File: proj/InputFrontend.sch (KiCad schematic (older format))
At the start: 22 parts

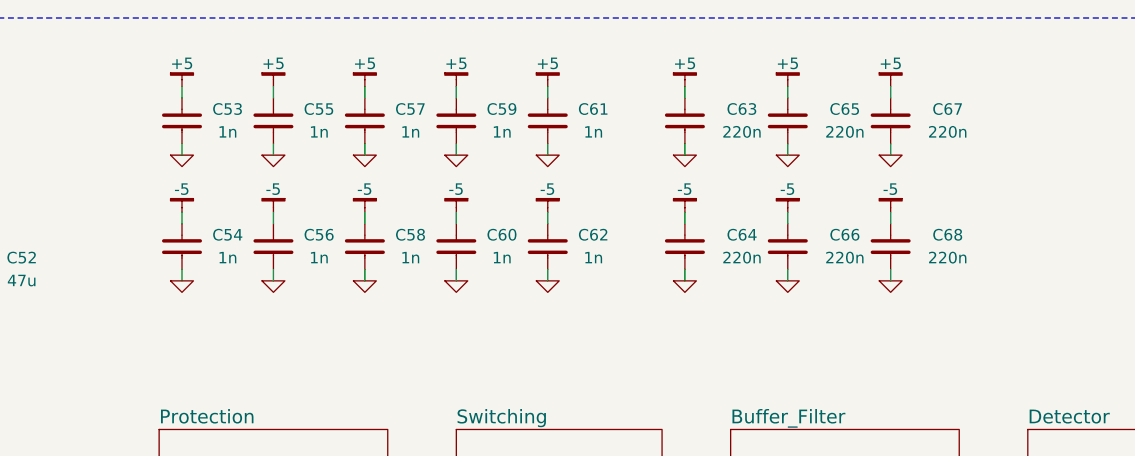
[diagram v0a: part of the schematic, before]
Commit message: All parts placed
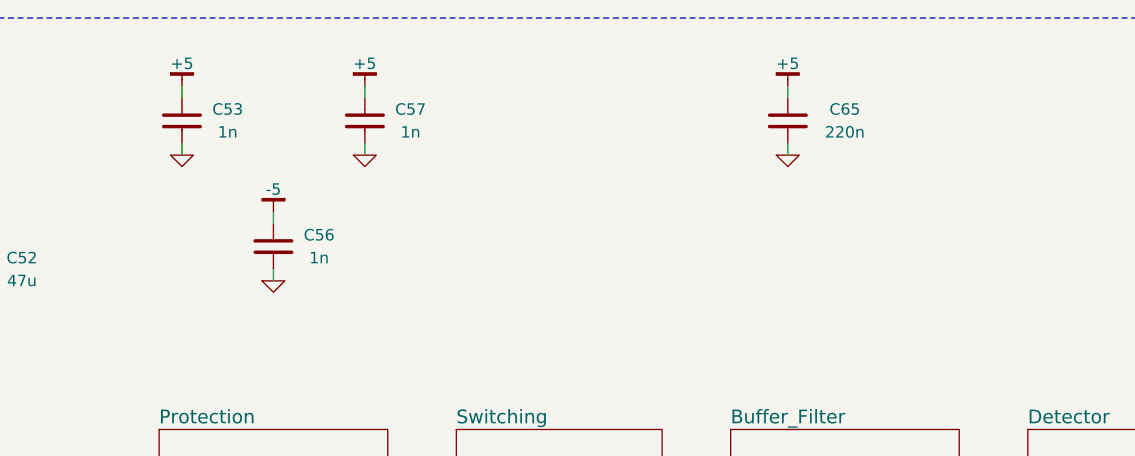
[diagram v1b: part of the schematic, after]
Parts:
- removed C54, C55, C58, C59, C60, C61, C62: 1n, IPC7351-Nominal:CAPC1005X55, symbol C-0402
- removed C63, C64, C66, C67, C68: 220n, IPC7351-Nominal:CAPC2012X70, symbol C-0805

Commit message: Major layout work - almost done
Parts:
- removed C56, C57: 1n, IPC7351-Nominal:CAPC1005X55, symbol C-0402
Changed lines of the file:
@@
 	3500 2450 3500 2400
-$Comp
-L C-0402 C56
-U 1 1 54F286AA
-P 4800 2200
-F 0 "C56" H 5000 2250 50  0000 C CNN
-F 1 "1n" H 5000 2150 50  0000 C CNN
-F 2 "IPC7351-Nominal:CAPC1005X55" H 4800 2200 50  0001 C CNN
-F 3 "" H 4790 2175 60  0000 C CNN
-F 4 "Value" H 4800 2200 60  0001 C CNN "Manuf"
-F 5 "CAP MLCC 1nF C0G 10V 5% [0402]" H 5600 2750 60  0001 C CNN "BOM"
-	1    4800 2200
-	1    0    0    -1
-$EndComp
-$Comp
-L -5 #PWR0183
-U 1 1 54F286B0
-P 4800 2050
-F 0 "#PWR0183" H 4800 2000 30  0001 C CNN
-F 1 "-5" H 4800 1950 50  0000 C CNN
-F 2 "" H 4800 2050 60  0000 C CNN
-F 3 "" H 4800 2050 60  0000 C CNN
-	1    4800 2050
-	-1   0    0    1
-$EndComp
-Wire Wire Line
-	4800 2050 4800 2100
-$Comp
-L GND #PWR0184
-U 1 1 54F286B7
-P 4800 2350
-F 0 "#PWR0184" H 4800 2350 30  0001 C CNN
-F 1 "GND" H 4800 2280 30  0001 C CNN
-F 2 "" H 4800 2350 60  0000 C CNN
-F 3 "" H 4800 2350 60  0000 C CNN
-	1    4800 2350
-	1    0    0    -1
-$EndComp
-Wire Wire Line
-	4800 2350 4800 2300
 $Comp
 L C-0402 C53
@@
 	4400 1500 4400 1550
 $Comp
-L GND #PWR0191
+L GND #PWR0181
 U 1 1 54F288BE
 P 4400 1800
-F 0 "#PWR0191" H 4400 1800 30  0001 C CNN
+F 0 "#PWR0181" H 4400 1800 30  0001 C CNN
 F 1 "GND" H 4400 1730 30  0001 C CNN
 F 2 "" H 4400 1800 60  0000 C CNN
@@
 	4400 1800 4400 1750
 $Comp
-L +5 #PWR0192
+L +5 #PWR0182
 U 1 1 54F2892E
 P 4400 1500
-F 0 "#PWR0192" H 4400 1550 30  0001 C CNN
+F 0 "#PWR0182" H 4400 1550 30  0001 C CNN
 F 1 "+5" H 4400 1600 50  0000 C CNN
 F 2 "" H 4400 1500 60  0000 C CNN
 F 3 "" H 4400 1500 60  0000 C CNN
 	1    4400 1500
-	1    0    0    -1
-$EndComp
-$Comp
-L C-0402 C57
-U 1 1 54F28B5B
-P 5200 1650
-F 0 "C57" H 5400 1700 50  0000 C CNN
-F 1 "1n" H 5400 1600 50  0000 C CNN
-F 2 "IPC7351-Nominal:CAPC1005X55" H 5200 1650 50  0001 C CNN
-F 3 "" H 5190 1625 60  0000 C CNN
-F 4 "Value" H 5200 1650 60  0001 C CNN "Manuf"
-F 5 "CAP MLCC 1nF C0G 10V 5% [0402]" H 6000 2200 60  0001 C CNN "BOM"
-	1    5200 1650
-	1    0    0    -1
-$EndComp
-Wire Wire Line
-	5200 1500 5200 1550
-$Comp
-L GND #PWR0195
-U 1 1 54F28B62
-P 5200 1800
-F 0 "#PWR0195" H 5200 1800 30  0001 C CNN
-F 1 "GND" H 5200 1730 30  0001 C CNN
-F 2 "" H 5200 1800 60  0000 C CNN
-F 3 "" H 5200 1800 60  0000 C CNN
-	1    5200 1800
-	1    0    0    -1
-$EndComp
-Wire Wire Line
-	5200 1800 5200 1750
-$Comp
-L +5 #PWR0196
-U 1 1 54F28B69
-P 5200 1500
-F 0 "#PWR0196" H 5200 1550 30  0001 C CNN
-F 1 "+5" H 5200 1600 50  0000 C CNN
-F 2 "" H 5200 1500 60  0000 C CNN
-F 3 "" H 5200 1500 60  0000 C CNN
-	1    5200 1500
 	1    0    0    -1
 $EndComp
@@
 	7050 1500 7050 1550
 $Comp
-L GND #PWR0209
+L GND #PWR0183
 U 1 1 54F29C50
 P 7050 1800
-F 0 "#PWR0209" H 7050 1800 30  0001 C CNN
+F 0 "#PWR0183" H 7050 1800 30  0001 C CNN
 F 1 "GND" H 7050 1730 30  0001 C CNN
 F 2 "" H 7050 1800 60  0000 C CNN
@@
 	7050 1800 7050 1750
 $Comp
-L +5 #PWR0210
+L +5 #PWR0184
 U 1 1 54F29C57
 P 7050 1500
-F 0 "#PWR0210" H 7050 1550 30  0001 C CNN
+F 0 "#PWR0184" H 7050 1550 30  0001 C CNN
 F 1 "+5" H 7050 1600 50  0000 C CNN
 F 2 "" H 7050 1500 60  0000 C CNN

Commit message: Swap 0402 to 0603, add USB inrush protection
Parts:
- removed C53, C69, C70: 1n, IPC7351-Nominal:CAPC1005X55, symbol C-0402
- removed R52, R53: 49R9, IPC7351-Nominal:RESC1005X40, symbol R-0402
- added C53: 1n, IPC7351-Nominal:CAPC1608X55, symbol C-0603
- added C69, C70: 10n, IPC7351-Nominal:CAPC1608X55, symbol C-0603
- added R52, R53: 49R9, IPC7351-Nominal:RESC1608X50, symbol R-0603
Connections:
- net +5: now also C53.1
- net Detector/OUT: now also R52.2
- net GND: now also C53.2, C69.2, C70.2
- net OUT: now also R53.1
- new net: C69.1, C70.1, R52.1, R53.2
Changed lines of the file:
@@
 $EndComp
 $Comp
-L GND #PWR0154
+L GND #PWR0147
 U 1 1 54F2F4A0
 P 3500 4300
-F 0 "#PWR0154" H 3500 4300 30  0001 C CNN
+F 0 "#PWR0147" H 3500 4300 30  0001 C CNN
 F 1 "GND" H 3500 4230 30  0001 C CNN
 F 2 "" H 3500 4300 60  0000 C CNN
@@
 Wire Notes Line
 	10300 1200 3200 1200
-$Comp
-L R-0402 R52
-U 1 1 54F300EB
-P 9600 3400
-F 0 "R52" V 9400 3400 50  0000 C CNN
-F 1 "49R9" V 9500 3400 50  0000 C CNN
-F 2 "IPC7351-Nominal:RESC1005X40" H 9600 3400 50  0001 C CNN
-F 3 "" H 9600 3450 60  0000 C CNN
-F 4 "Value" H 9600 3400 60  0001 C CNN "Manuf"
-F 5 "RES SMD 49R9 1% [0402]" H 10350 3950 60  0001 C CNN "BOM"
-	1    9600 3400
-	0    1    1    0
-$EndComp
-$Comp
-L C-0402 C69
-U 1 1 54F3060B
-P 9800 3600
-F 0 "C69" H 10000 3650 50  0000 C CNN
-F 1 "1n" H 10000 3550 50  0000 C CNN
-F 2 "IPC7351-Nominal:CAPC1005X55" H 9800 3600 50  0001 C CNN
-F 3 "" H 9790 3575 60  0000 C CNN
-F 4 "Value" H 9800 3600 60  0001 C CNN "Manuf"
-F 5 "CAP MLCC 1nF C0G 10V 5% [0402]" H 10600 4150 60  0001 C CNN "BOM"
-	1    9800 3600
-	1    0    0    -1
-$EndComp
 Wire Wire Line
 	9700 3400 10800 3400
@@
 	9800 3400 9800 3500
 Connection ~ 9800 3400
-$Comp
-L C-0402 C70
-U 1 1 54F3063B
-P 10700 3600
-F 0 "C70" H 10900 3650 50  0000 C CNN
-F 1 "1n" H 10900 3550 50  0000 C CNN
-F 2 "IPC7351-Nominal:CAPC1005X55" H 10700 3600 50  0001 C CNN
-F 3 "" H 10690 3575 60  0000 C CNN
-F 4 "Value" H 10700 3600 60  0001 C CNN "Manuf"
-F 5 "CAP MLCC 1nF C0G 10V 5% [0402]" H 11500 4150 60  0001 C CNN "BOM"
-	1    10700 3600
-	1    0    0    -1
-$EndComp
 Wire Wire Line
 	10700 3400 10700 3500
-$Comp
-L R-0402 R53
-U 1 1 54F30671
-P 10900 3400
-F 0 "R53" V 10700 3400 50  0000 C CNN
-F 1 "49R9" V 10800 3400 50  0000 C CNN
-F 2 "IPC7351-Nominal:RESC1005X40" H 10900 3400 50  0001 C CNN
-F 3 "" H 10900 3450 60  0000 C CNN
-F 4 "Value" H 10900 3400 60  0001 C CNN "Manuf"
-F 5 "RES SMD 49R9 1% [0402]" H 11650 3950 60  0001 C CNN "BOM"
-	1    10900 3400
-	0    1    1    0
-$EndComp
 Connection ~ 10700 3400
 Text HLabel 11600 3400 2    60   Output ~ 0
@@
 	11600 3400 11000 3400
 $Comp
-L GND #PWR0155
+L GND #PWR0148
 U 1 1 54F3075A
 P 9800 3800
-F 0 "#PWR0155" H 9800 3800 30  0001 C CNN
+F 0 "#PWR0148" H 9800 3800 30  0001 C CNN
 F 1 "GND" H 9800 3730 30  0001 C CNN
 F 2 "" H 9800 3800 60  0000 C CNN
@@
 	9800 3700 9800 3800
 $Comp
-L GND #PWR0156
+L GND #PWR0149
 U 1 1 54F3079D
 P 10700 3800
-F 0 "#PWR0156" H 10700 3800 30  0001 C CNN
+F 0 "#PWR0149" H 10700 3800 30  0001 C CNN
 F 1 "GND" H 10700 3730 30  0001 C CNN
 F 2 "" H 10700 3800 60  0000 C CNN
@@
 $EndComp
 $Comp
-L -5 #PWR0157
+L -5 #PWR0150
 U 1 1 54F26D5C
 P 3500 2150
-F 0 "#PWR0157" H 3500 2100 30  0001 C CNN
+F 0 "#PWR0150" H 3500 2100 30  0001 C CNN
 F 1 "-5" H 3500 2050 50  0000 C CNN
 F 2 "" H 3500 2150 60  0000 C CNN
@@
 	3500 2150 3500 2200
 $Comp
-L GND #PWR0158
+L GND #PWR0151
 U 1 1 54F26E11
 P 3500 2450
-F 0 "#PWR0158" H 3500 2450 30  0001 C CNN
+F 0 "#PWR0151" H 3500 2450 30  0001 C CNN
 F 1 "GND" H 3500 2380 30  0001 C CNN
 F 2 "" H 3500 2450 60  0000 C CNN
@@
 Wire Wire Line
 	3500 2450 3500 2400
-$Comp
-L C-0402 C53
-U 1 1 54F288B1
-P 4400 1650
-F 0 "C53" H 4600 1700 50  0000 C CNN
-F 1 "1n" H 4600 1600 50  0000 C CNN
-F 2 "IPC7351-Nominal:CAPC1005X55" H 4400 1650 50  0001 C CNN
-F 3 "" H 4390 1625 60  0000 C CNN
-F 4 "Value" H 4400 1650 60  0001 C CNN "Manuf"
-F 5 "CAP MLCC 1nF C0G 10V 5% [0402]" H 5200 2200 60  0001 C CNN "BOM"
-	1    4400 1650
-	1    0    0    -1
-$EndComp
 Wire Wire Line
 	4400 1500 4400 1550
 $Comp
-L GND #PWR0159
+L GND #PWR0152
 U 1 1 54F288BE
 P 4400 1800
-F 0 "#PWR0159" H 4400 1800 30  0001 C CNN
+F 0 "#PWR0152" H 4400 1800 30  0001 C CNN
 F 1 "GND" H 4400 1730 30  0001 C CNN
 F 2 "" H 4400 1800 60  0000 C CNN
@@
 	4400 1800 4400 1750
 $Comp
-L +5 #PWR0160
+L +5 #PWR0153
 U 1 1 54F2892E
 P 4400 1500
-F 0 "#PWR0160" H 4400 1550 30  0001 C CNN
+F 0 "#PWR0153" H 4400 1550 30  0001 C CNN
 F 1 "+5" H 4400 1600 50  0000 C CNN
 F 2 "" H 4400 1500 60  0000 C CNN
@@
 	7050 1500 7050 1550
 $Comp
-L GND #PWR0161
+L GND #PWR0154
 U 1 1 54F29C50
 P 7050 1800
-F 0 "#PWR0161" H 7050 1800 30  0001 C CNN
+F 0 "#PWR0154" H 7050 1800 30  0001 C CNN
 F 1 "GND" H 7050 1730 30  0001 C CNN
 F 2 "" H 7050 1800 60  0000 C CNN
@@
 	7050 1800 7050 1750
 $Comp
-L +5 #PWR0162
+L +5 #PWR0155
 U 1 1 54F29C57
 P 7050 1500
-F 0 "#PWR0162" H 7050 1550 30  0001 C CNN
+F 0 "#PWR0155" H 7050 1550 30  0001 C CNN
 F 1 "+5" H 7050 1600 50  0000 C CNN
 F 2 "" H 7050 1500 60  0000 C CNN
@@
 	1    0    0    -1
 $EndComp
+$Comp
+L C-0603 C53
+U 1 1 5502DDEE
+P 4400 1650
+F 0 "C53" H 4600 1700 50  0000 C CNN
+F 1 "1n" H 4600 1600 50  0000 C CNN
+F 2 "IPC7351-Nominal:CAPC1608X55" H 4400 1650 50  0001 C CNN
+F 3 "" H 4390 1625 60  0000 C CNN
+F 4 "Value" H 4400 1650 60  0001 C CNN "Manuf"
+F 5 "CAP MLCC 1n C0G 50V 10% [0603]" H 5200 2200 60  0001 C CNN "BOM"
+	1    4400 1650
+	1    0    0    -1
+$EndComp
+$Comp
+L C-0603 C69
+U 1 1 55033561
+P 9800 3600
+F 0 "C69" H 10000 3650 50  0000 C CNN
+F 1 "10n" H 10000 3550 50  0000 C CNN
+F 2 "IPC7351-Nominal:CAPC1608X55" H 9800 3600 50  0001 C CNN
+F 3 "" H 9790 3575 60  0000 C CNN
+F 4 "Value" H 9800 3600 60  0001 C CNN "Manuf"
+F 5 "CAP MLCC 10n ≥X5R 50V 10% [0603]" H 10600 4150 60  0001 C CNN "BOM"
+	1    9800 3600
+	1    0    0    -1
+$EndComp
+$Comp
+L C-0603 C70
+U 1 1 55033D91
+P 10700 3600
+F 0 "C70" H 10900 3650 50  0000 C CNN
+F 1 "10n" H 10900 3550 50  0000 C CNN
+F 2 "IPC7351-Nominal:CAPC1608X55" H 10700 3600 50  0001 C CNN
+F 3 "" H 10690 3575 60  0000 C CNN
+F 4 "Value" H 10700 3600 60  0001 C CNN "Manuf"
+F 5 "CAP MLCC 10n ≥X5R 50V 10% [0603]" H 11500 4150 60  0001 C CNN "BOM"
+	1    10700 3600
+	1    0    0    -1
+$EndComp
+$Comp
+L R-0603 R52
+U 1 1 55033DF8
+P 9600 3400
+F 0 "R52" V 9400 3400 50  0000 C CNN
+F 1 "49R9" V 9500 3400 50  0000 C CNN
+F 2 "IPC7351-Nominal:RESC1608X50" H 9600 3400 50  0001 C CNN
+F 3 "" H 9600 3450 60  0000 C CNN
+F 4 "Value" H 9600 3400 60  0001 C CNN "Manuf"
+F 5 "RES SMD 49R9 1% [0603]" H 10350 3950 60  0001 C CNN "BOM"
+	1    9600 3400
+	0    1    1    0
+$EndComp
+$Comp
+L R-0603 R53
+U 1 1 550340A6
+P 10900 3400
+F 0 "R53" V 10700 3400 50  0000 C CNN
+F 1 "49R9" V 10800 3400 50  0000 C CNN
+F 2 "IPC7351-Nominal:RESC1608X50" H 10900 3400 50  0001 C CNN
+F 3 "" H 10900 3450 60  0000 C CNN
+F 4 "Value" H 10900 3400 60  0001 C CNN "Manuf"
+F 5 "RES SMD 49R9 1% [0603]" H 11650 3950 60  0001 C CNN "BOM"
+	1    10900 3400
+	0    1    1    0
+$EndComp
 $EndSCHEMATC
